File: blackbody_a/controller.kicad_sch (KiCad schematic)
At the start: 0 parts

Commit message: Added controller and CAN
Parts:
- added C2, C3: 12p, symbol Device:C
- added C4: 4.7uF, symbol Device:C
- added C5, C6, C7, C8: 100nF, symbol Device:C
- added J2: Conn_01x04, symbol Connector_Generic:Conn_01x04
- added R3: 10k, symbol Device:R_US
- added SW1: Reset, symbol Switch:SW_Push
- added U2: STM32L432KCUx, Package_DFN_QFN:QFN-32-1EP_5x5mm_P0.5mm_EP3.45x3.45mm, symbol MCU_ST_STM32L4:STM32L432KCUx
- added Y1: 8M, symbol Device:Crystal
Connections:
- new net: C3.2, U2.3 (PC15), Y1.2
- new net: C2.2, U2.2 (PC14), Y1.1
- new net +3V3: C4.1, C5.1, C6.1, C7.1, J2.1 (Pin_1), R3.1, U2.1 (VDD), U2.17 (VDD), U2.5 (VDDA)
- new net CAN_RX: U2.21 (PA11), U2.9 (PA3)
- new net CAN_TX: U2.22 (PA12), U2.8 (PA2)
- new net Error: U2.7 (PA1)
- new net GND: C2.1, C3.1, C4.2, C5.2, C6.2, C7.2, C8.1, J2.4 (Pin_4), SW1.2, U2.16 (VSS), U2.31 (PH3), U2.32 (VSS), U2.33 (VSS)
- new net Heartbeat: U2.6 (PA0)
- new net I2C: U2.10 (PA4)
- new net I2C1_SCL: U2.27 (PB4)
- new net I2C1_SDA: U2.28 (PB5)
- new net I2C2_SCL: U2.20 (PA10)
- new net I2C2_SDA: U2.19 (PA9)
- new net NRST: C8.2, R3.2, SW1.1, U2.4 (NRST)
- new net SWCLK: J2.3 (Pin_3), U2.24 (PA14)
- new net SWDIO: J2.2 (Pin_2), U2.23 (PA13)
- no-connect marks 0 -> 9
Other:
- note added: "Bypass Capacitors"
- note added: "Controller"
- note added: "Reset Button"

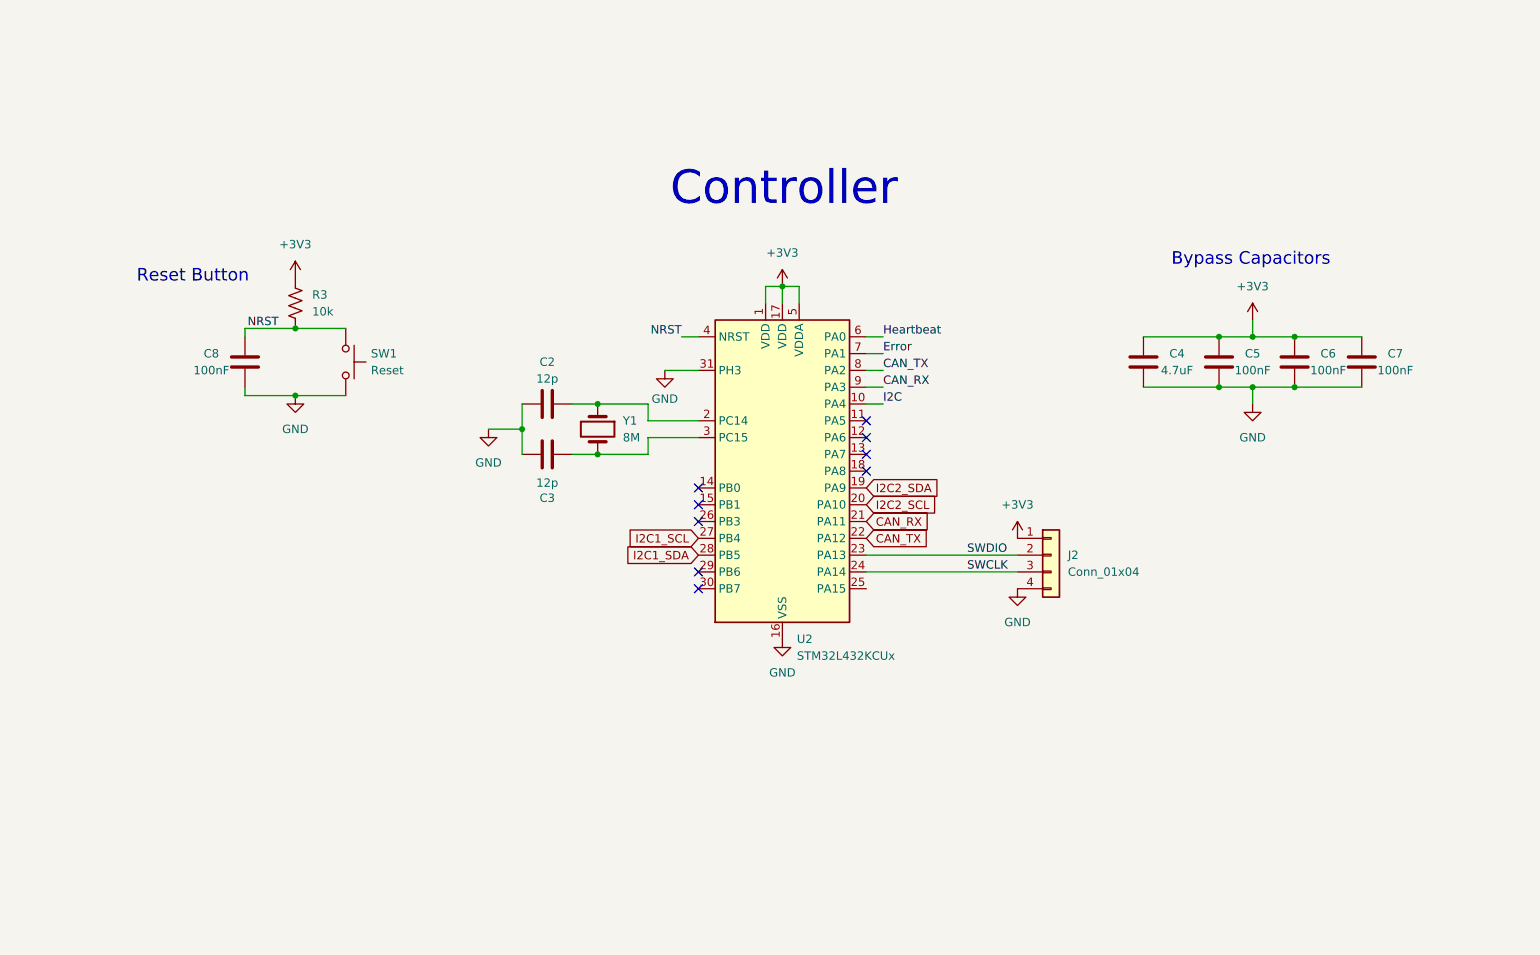
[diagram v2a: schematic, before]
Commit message: Added power distribution
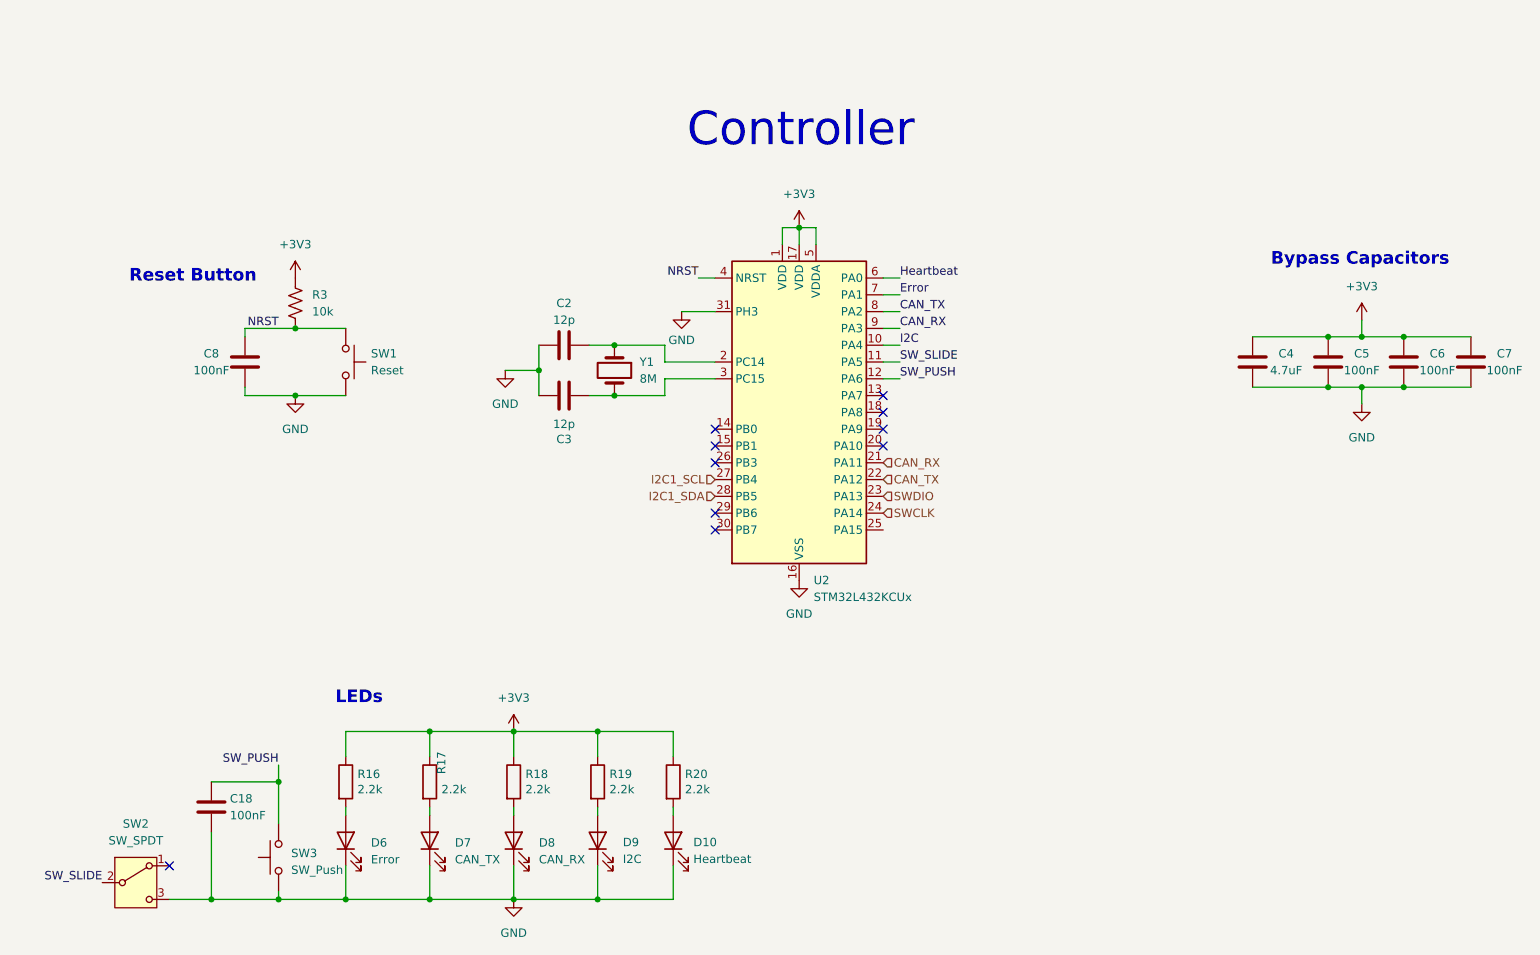
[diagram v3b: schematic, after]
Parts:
- removed J2: Conn_01x04, symbol Connector_Generic:Conn_01x04
- added C18: 100nF, Capacitor_SMD:C_0805_2012Metric, symbol Device:C
- added D10: Heartbeat, LED_SMD:LED_0805_2012Metric, symbol Device:LED
- added D6: Error, LED_SMD:LED_0805_2012Metric, symbol Device:LED
- added D7: CAN_TX, LED_SMD:LED_0805_2012Metric, symbol Device:LED
- added D8: CAN_RX, LED_SMD:LED_0805_2012Metric, symbol Device:LED
- added D9: I2C, LED_SMD:LED_0805_2012Metric, symbol Device:LED
- added R16, R17, R18, R19, R20: 2.2k, Resistor_SMD:R_0805_2012Metric, symbol Device:R
- added SW2: SW_SPDT, symbol Switch:SW_SPDT
- added SW3: SW_Push, Button_Switch_SMD:SW_SPST_B3SL-1002P, symbol Switch:SW_Push
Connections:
- net +3V3: now also R16.1, R17.1, R18.1, R19.1, R20.1
- net GND: now also C18.2, D10.1 (K), D6.1 (K), D7.1 (K), D8.1 (K), D9.1 (K), SW2.3 (C), SW3.1
- net SW_SLIDE: now reaches U2.11 (PA5)
- net SW_SLIDE: now also SW2.2 (B)
- net SW_PUSH: now reaches U2.12 (PA6)
- net SW_PUSH: now also C18.1, SW3.2
- net I2C2_SCL: no longer names the net of U2.20 (PA10)
- net I2C2_SDA: no longer names the net of U2.19 (PA9)
- new net: D9.2 (A), R19.2
- new net: D8.2 (A), R18.2
- new net: D10.2 (A), R20.2
- new net: D6.2 (A), R16.2
- new net: D7.2 (A), R17.2
- no-connect marks 9 -> 10
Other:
- note added: "LEDs"
- moved on the sheet: C2, C3, C4, C5, C6, C7, U2, Y1

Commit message: minor errors
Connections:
- net +3V3: no longer R16.1, R17.1, R18.1, R19.1, R20.1
- net CAN_RX: now also R18.1
- net CAN_TX: now also R17.1
- net Error: now also R16.1
- net Heartbeat: now also R20.1
- net I2C: now also R19.1
- no-connect marks 10 -> 11
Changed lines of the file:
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@@
-	)
-	(junction
-		(at 109.22 139.7)
-		(diameter 0)
-		(color 0 0 0 0)
 	)
 	(junction
@@
 	)
 	(junction
-		(at 83.82 139.7)
-		(diameter 0)
-		(color 0 0 0 0)
-	)
-	(junction
 		(at 224.79 80.01)
 		(diameter 0)
@@
 	(junction
 		(at 219.71 87.63)
-		(diameter 0)
-		(color 0 0 0 0)
-	)
-	(junction
-		(at 96.52 139.7)
 		(diameter 0)
 		(color 0 0 0 0)
@@
 		(at 127 93.98)
 	)
+	(no_connect
+		(at 152.4 109.22)
+	)
 	(wire
 		(pts
@@
 	(wire
 		(pts
-			(xy 71.12 139.7) (xy 83.82 139.7)
-		)
-		(stroke
-			(width 0)
-			(type default)
-		)
-	)
-	(wire
-		(pts
 			(xy 107.95 81.28) (xy 111.76 81.28)
 		)
@@
 	(wire
 		(pts
-			(xy 109.22 139.7) (xy 120.65 139.7)
-		)
-		(stroke
-			(width 0)
-			(type default)
-		)
-	)
-	(wire
-		(pts
-			(xy 83.82 139.7) (xy 96.52 139.7)
-		)
-		(stroke
-			(width 0)
-			(type default)
-		)
-	)
-	(wire
-		(pts
 			(xy 109.22 160.02) (xy 109.22 165.1)
 		)
@@
 		(pts
 			(xy 83.82 139.7) (xy 83.82 143.51)
-		)
-		(stroke
-			(width 0)
-			(type default)
-		)
-	)
-	(wire
-		(pts
-			(xy 96.52 139.7) (xy 109.22 139.7)
 		)
 		(stroke
@@
 		)
 	)
+	(label "CAN_TX"
+		(at 83.82 139.7 0)
+		(fields_autoplaced yes)
+		(effects
+			(font
+				(size 1.27 1.27)
+			)
+			(justify left bottom)
+		)
+	)
 	(label "Heartbeat"
 		(at 154.94 71.12 0)
@@
 		)
 	)
+	(label "CAN_RX"
+		(at 96.52 139.7 0)
+		(fields_autoplaced yes)
+		(effects
+			(font
+				(size 1.27 1.27)
+			)
+			(justify left bottom)
+		)
+	)
+	(label "Error"
+		(at 71.12 139.7 0)
+		(fields_autoplaced yes)
+		(effects
+			(font
+				(size 1.27 1.27)
+			)
+			(justify left bottom)
+		)
+	)
 	(label "SW_SLIDE"
 		(at 34.29 162.56 180)
@@
 	(label "CAN_RX"
 		(at 154.94 78.74 0)
+		(fields_autoplaced yes)
+		(effects
+			(font
+				(size 1.27 1.27)
+			)
+			(justify left bottom)
+		)
+	)
+	(label "Heartbeat"
+		(at 120.65 139.7 0)
+		(fields_autoplaced yes)
+		(effects
+			(font
+				(size 1.27 1.27)
+			)
+			(justify left bottom)
+		)
+	)
+	(label "I2C"
+		(at 109.22 139.7 0)
 		(fields_autoplaced yes)
 		(effects
@@
 					(unit 1)
 				)
-			)
-		)
-	)
-	(symbol
-		(lib_id "power:+3V3")
-		(at 96.52 139.7 0)
-		(unit 1)
-		(exclude_from_sim no)
-		(in_bom yes)
-		(on_board yes)
-		(dnp no)
-		(fields_autoplaced yes)
-		(property "Reference" "#PWR041"
-			(at 96.52 143.51 0)
-			(effects
-				(font
-					(size 1.27 1.27)
-				)
-				(hide yes)
-			)
-		)
-		(property "Value" "+3V3"
-			(at 96.52 134.62 0)
-			(effects
-				(font
-					(size 1.27 1.27)
-				)
-			)
-		)
-		(property "Footprint" ""
-			(at 96.52 139.7 0)
-			(effects
-				(font
-					(size 1.27 1.27)
-				)
-				(hide yes)
-			)
-		)
-		(property "Datasheet" ""
-			(at 96.52 139.7 0)
-			(effects
-				(font
-					(size 1.27 1.27)
-				)
-				(hide yes)
-			)
-		)
-		(property "Description" "Power symbol creates a global label with name \"+3V3\""
-			(at 96.52 139.7 0)
-			(effects
-				(font
-					(size 1.27 1.27)
-				)
-				(hide yes)
-			)
-		)
-		(pin "1"
-		)
-		(instances
-			(project "blackbody_a"
-				(path "/1fc8ae43-742a-46b6-a93b-79253d0d0202/f9bf57dd-4a71-43f1-9ea2-c0c5623cdce8"
-					(reference "#PWR041")
-					(unit 1)
-				)

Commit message: Fixed pins, minor changes, removed power isolation
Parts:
- removed C2, C3: 12p, symbol Device:C
- removed D7: CAN_TX, LED_SMD:LED_0805_2012Metric, symbol Device:LED
- removed D8: CAN_RX, LED_SMD:LED_0805_2012Metric, symbol Device:LED
- removed R17, R18: 2.2k, Resistor_SMD:R_0805_2012Metric, symbol Device:R
- removed U2: STM32L432KCUx, Package_DFN_QFN:QFN-32-1EP_5x5mm_P0.5mm_EP3.45x3.45mm, symbol MCU_ST_STM32L4:STM32L432KCUx
- removed Y1: 8M, symbol Device:Crystal
- added C16, C17: 12p, symbol Device:C
- added U4: STM32L431CBTx, Package_QFP:LQFP-48_7x7mm_P0.5mm, symbol MCU_ST_STM32L4:STM32L431CBTx
- added Y2: 8M, symbol Device:Crystal
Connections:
- net +3V3: now also U4.24 (VDD), U4.36 (VDD), U4.48 (VDD), U4.9 (VDDA)
- net CAN_RX: now also U4.32 (PA11)
- net CAN_TX: now also U4.33 (PA12)
- net Error: now also U4.11 (PA1)
- net GND: now also C16.1, C17.1, U4.23 (VSS), U4.35 (VSS), U4.44 (PH3), U4.47 (VSS), U4.8 (VSSA)
- net Heartbeat: now also U4.10 (PA0)
- net I2C: now also U4.12 (PA2)
- net I2C1_SCL: now also U4.42 (PB6)
- net I2C1_SDA: now also U4.43 (PB7)
- net NRST: now also U4.7 (NRST)
- net SWCLK: now also U4.37 (PA14)
- net SWDIO: now also U4.34 (PA13)
- net SW_PUSH: now also U4.14 (PA4)
- net SW_SLIDE: now also U4.13 (PA3)
- new net: C17.2, U4.6 (PH1), Y2.2
- new net: C16.2, U4.5 (PH0), Y2.1
- no-connect marks 11 -> 26
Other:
- moved on the sheet: C18, D10, D9, R19, R20, SW2, SW3
